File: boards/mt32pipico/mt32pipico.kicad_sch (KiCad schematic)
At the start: 21 parts, among them J1 PWRIN, J10 VBUS, J2 ToPi, J3 ToMiSTer, J4 Relay, J5 MiSTerLED, J6 MiSTerSwitch, J7 ADC, J8 IO, J9 SWD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

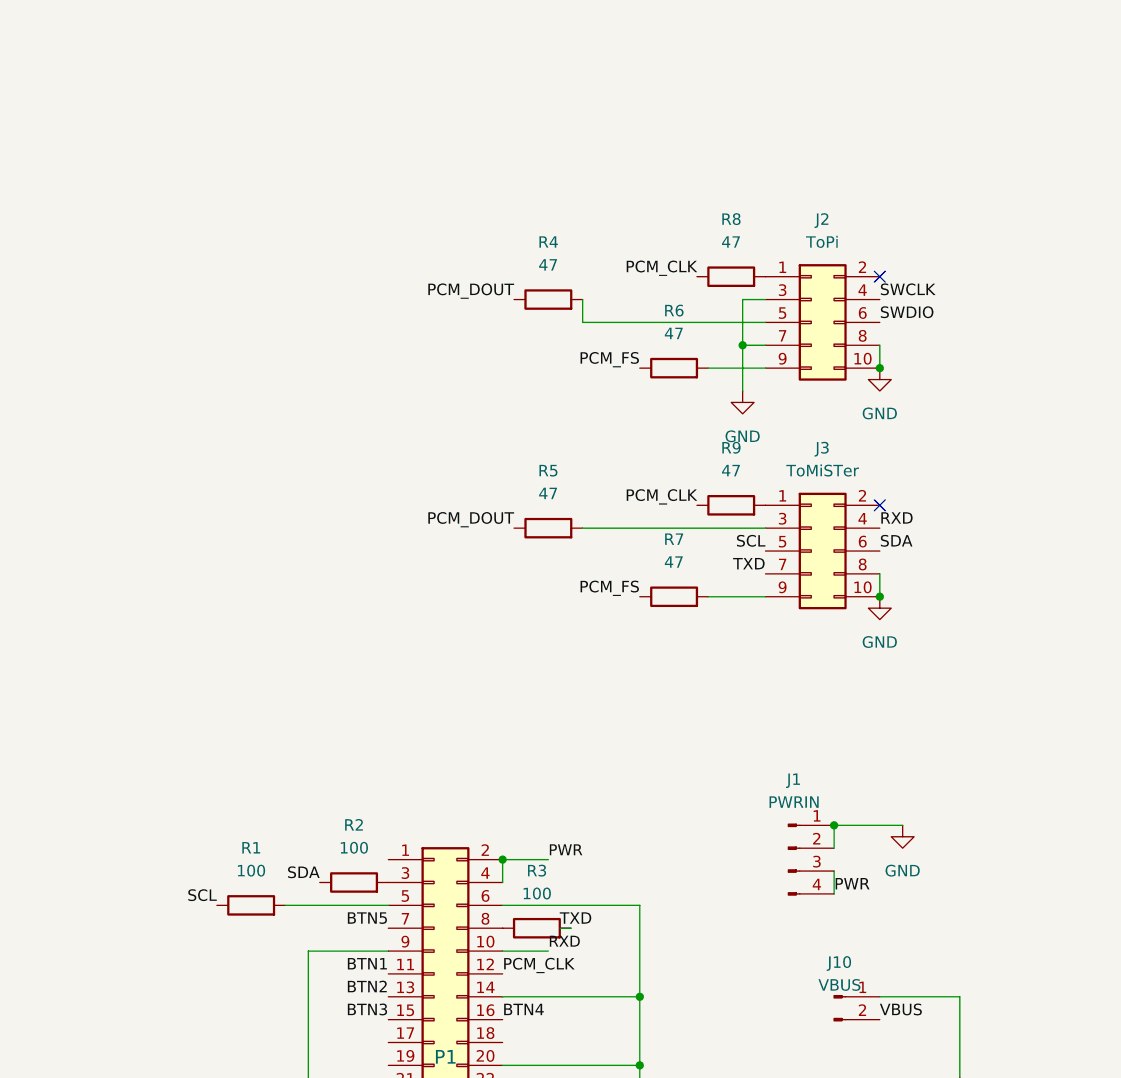
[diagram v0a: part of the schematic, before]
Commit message: Move to 14 pin headers for switch with off-board adapters
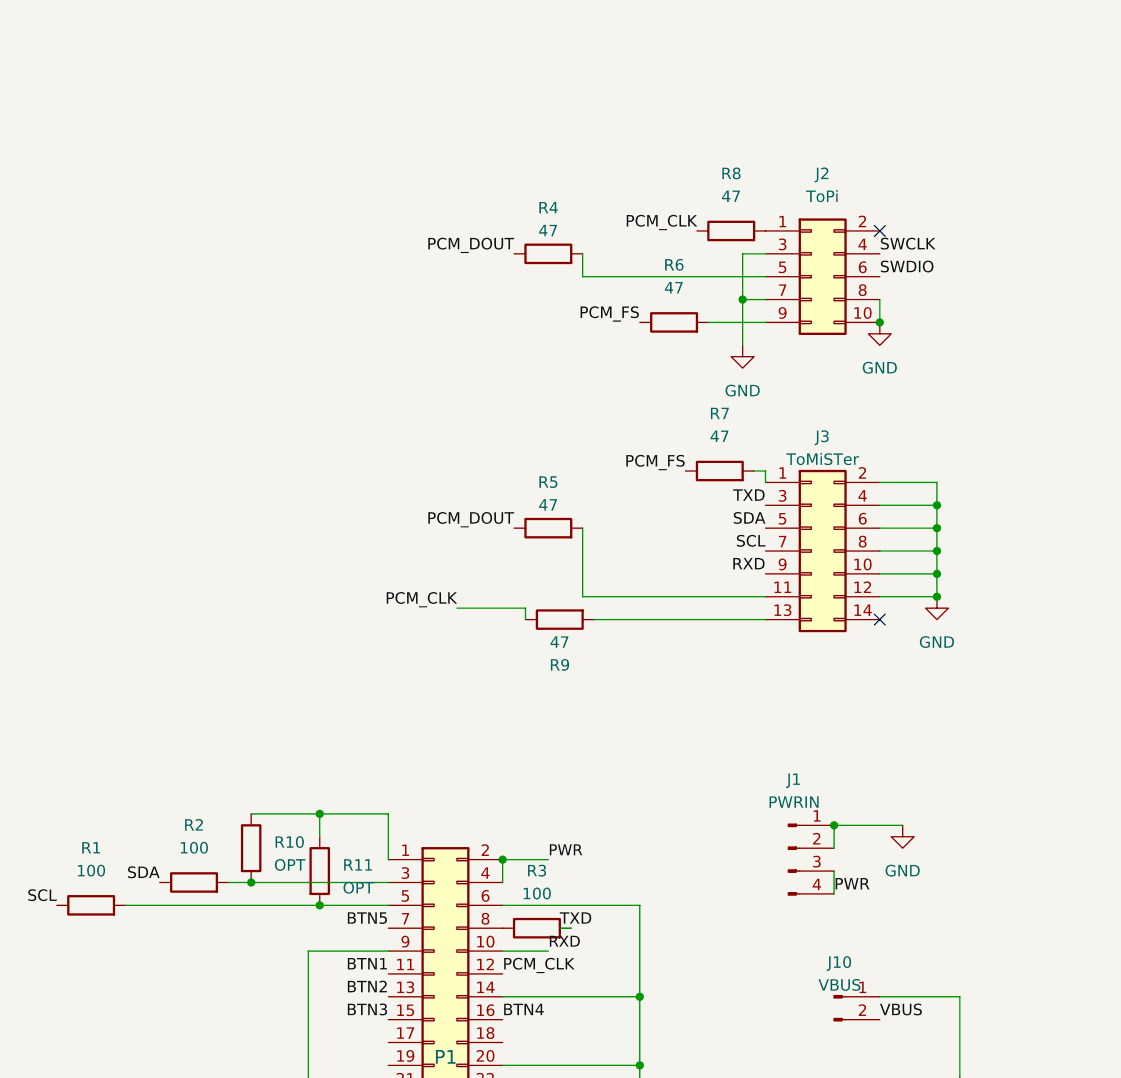
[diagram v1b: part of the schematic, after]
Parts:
- added R10, R11: OPT, Resistor_SMD:R_0805_2012Metric, symbol Device:R
- J3: footprint Connector_PinHeader_2.54mm:PinHeader_2x05_P2.54mm_Vertical -> Connector_PinHeader_2.54mm:PinHeader_2x07_P2.54mm_Vertical; symbol Connector_Generic:Conn_02x05_Odd_Even -> Connector_Generic:Conn_02x07_Odd_Even
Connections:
- net GND: now also J3.12 (Pin_12), J3.2 (Pin_2), J3.4 (Pin_4), J3.6 (Pin_6)
- net RXD: now also J3.9 (Pin_9); no longer J3.4 (Pin_4)
- net SCL: now also J3.7 (Pin_7); no longer J3.5 (Pin_5)
- net SDA: now also J3.5 (Pin_5); no longer J3.6 (Pin_6)
- net TXD: now also J3.3 (Pin_3); no longer J3.7 (Pin_7)
- net at P1.1 (Pin_1): now also R10.1, R11.1
- net at P1.3 (Pin_3), R2.2: now also R10.2
- net at P1.5 (Pin_5), R1.2: now also R11.2
- net at J3.1 (Pin_1): now also R7.2; no longer R9.2
- net at R5.2: now also J3.11 (Pin_11); no longer J3.3 (Pin_3)
- new net: J3.13 (Pin_13), R9.2
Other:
- moved on the sheet: J2, R1, R2, R4, R6, R7, R8, R9
